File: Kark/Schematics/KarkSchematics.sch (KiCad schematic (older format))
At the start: 33 parts

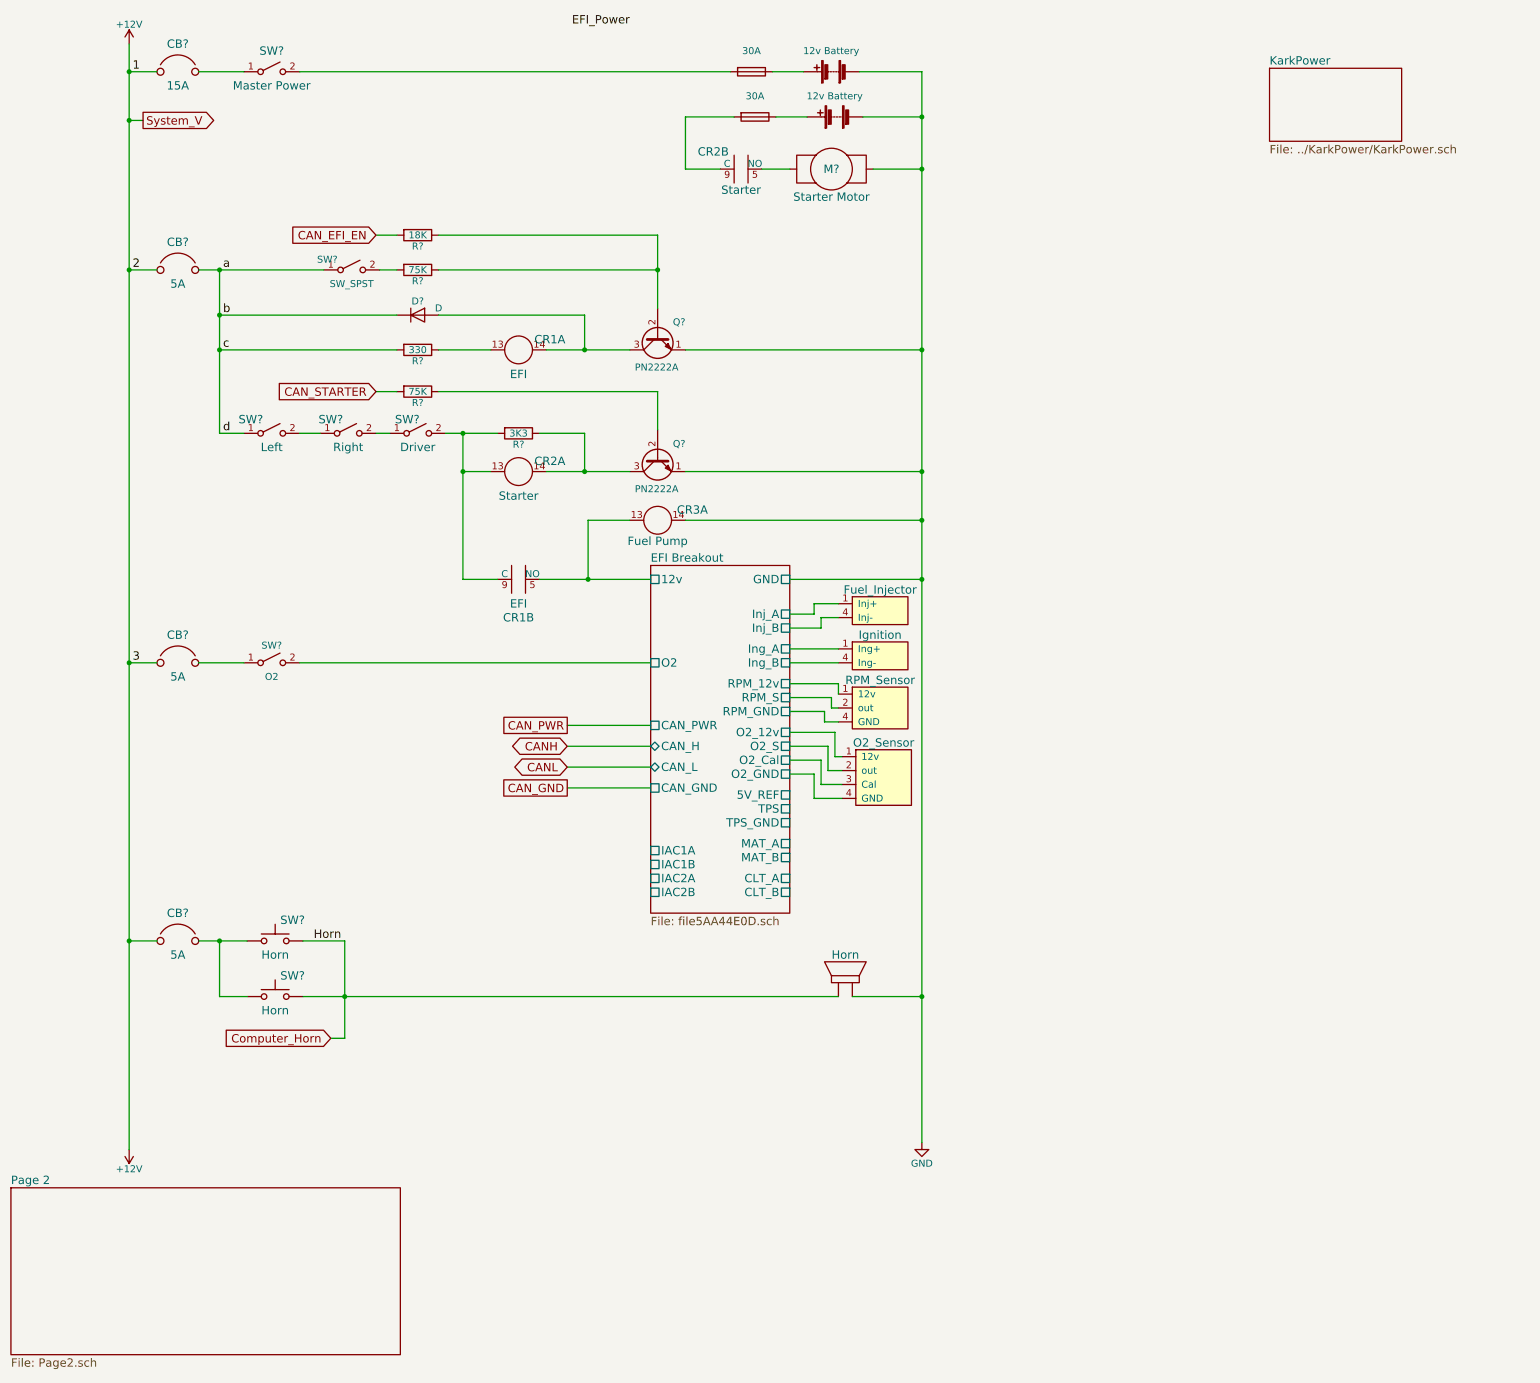
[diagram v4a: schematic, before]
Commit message: Created can breakout
Added can boards fro sensors and integrated the computer to the can system.
Created the Can powering system.
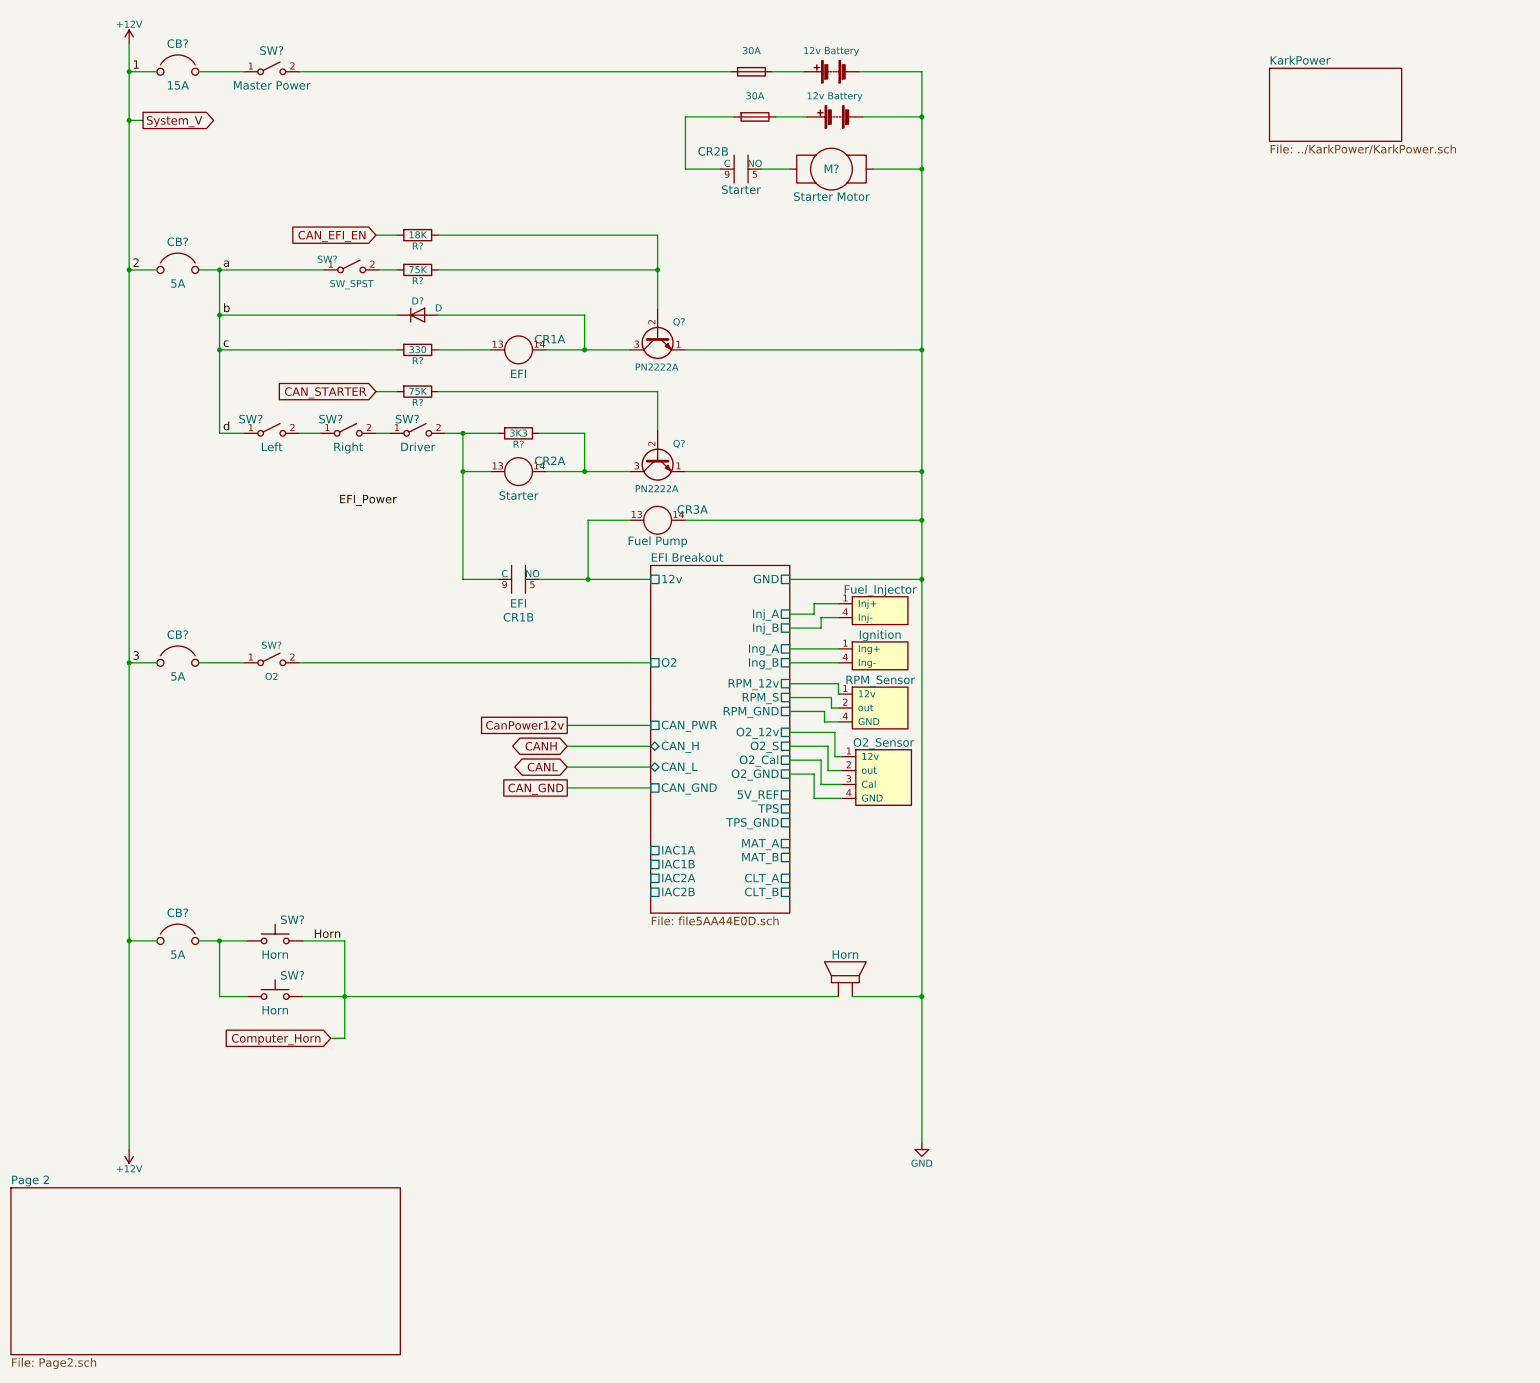
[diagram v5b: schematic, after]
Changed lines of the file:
@@
 LIBS:supermileage_computers
 LIBS:supermileage_sensors
+LIBS:EllicottDisplay
+LIBS:EllicottInterface
+LIBS:EllicottMicrocontrollers
+LIBS:EllicottMisc
+LIBS:EllicottPower
 LIBS:KarkSchematics-cache
 EELAYER 25 0
@@
 $Descr USLetter 8500 11000 portrait
 encoding utf-8
-Sheet 1 6
+Sheet 1 9
 Title "Kark - Gasoline Prototype"
 Date "2018-03-10"
@@
 Text Label 3025 7350 2    60   ~ 0
 Horn
-Text Label 5100 775  2    60   ~ 0
+Text Label 3425 4225 2    60   ~ 0
 EFI_Power
 $Sheet
@@
 CAN_GND
 Text GLabel 4650 5800 0    60   UnSpc ~ 0
-CAN_PWR
+CanPower12v
 Text GLabel 1600 1450 2    60   Output ~ 0
 System_V
@@
 Connection ~ 1500 2525
 Wire Wire Line
-	2150 2525 2150 2850
-Wire Wire Line
-	2150 2850 2150 3100
-Wire Wire Line
-	2150 3100 2150 3700
+	2150 2525 2150 3700
 Wire Wire Line
 	2750 7350 3050 7350
 Wire Wire Line
-	3050 7350 3050 7750
-Wire Wire Line
-	3050 7750 3050 8050
+	3050 7350 3050 8050
 Connection ~ 3050 7750
 Wire Wire Line
@@
 	6250 5350 6600 5350
 Wire Wire Line
-	2750 7750 3050 7750
-Wire Wire Line
-	3050 7750 6600 7750
+	2750 7750 6600 7750
 Wire Wire Line
 	7200 7750 6700 7750
 Wire Wire Line
-	7200 1100 7200 1425
-Wire Wire Line
-	7200 1425 7200 1800
-Wire Wire Line
-	7200 1800 7200 3100
-Wire Wire Line
-	7200 3100 7200 3975
-Wire Wire Line
-	7200 3975 7200 4325
-Wire Wire Line
-	7200 4325 7200 4750
-Wire Wire Line
-	7200 4750 7200 7750
-Wire Wire Line
-	7200 7750 7200 8800
+	7200 1100 7200 8800
 Wire Wire Line
 	5500 1800 5750 1800
@@
 Connection ~ 7200 1800
 Wire Wire Line
-	1500 900  1500 1100
-Wire Wire Line
-	1500 1100 1500 1450
-Wire Wire Line
-	1500 1450 1500 2525
-Wire Wire Line
-	1500 2525 1500 5350
-Wire Wire Line
-	1500 5350 1500 7350
-Wire Wire Line
-	1500 7350 1500 8850
+	1500 900  1500 8850
 Wire Wire Line
 	3050 8050 2950 8050
@@
 Connection ~ 1500 1450
 Wire Wire Line
-	3775 3700 3900 3700
-Wire Wire Line
-	3900 3700 4150 3700
+	3775 3700 4150 3700
 Wire Wire Line
 	3900 4750 4150 4750
@@
 	3425 3100 2150 3100
 Wire Wire Line
-	4500 3100 4775 3100
-Wire Wire Line
-	4775 3100 5100 3100
+	4500 3100 5100 3100
 Wire Wire Line
 	7200 3100 5500 3100
@@
 Connection ~ 4775 3100
 Wire Wire Line
-	2000 2525 2150 2525
-Wire Wire Line
-	2150 2525 2900 2525
+	2000 2525 2900 2525
 Wire Wire Line
 	3425 2525 3300 2525
@@
 	3725 2525 5300 2525
 Wire Wire Line
-	5300 2275 5300 2525
-Wire Wire Line
-	5300 2525 5300 2800
+	5300 2275 5300 2800
 Connection ~ 5300 2525
 Wire Wire Line
@@
 	2000 5350 2325 5350
 Wire Wire Line
-	2000 7350 2150 7350
-Wire Wire Line
-	2150 7350 2350 7350
+	2000 7350 2350 7350
 Wire Wire Line
 	1700 7350 1500 7350
@@
 $EndComp
 Wire Wire Line
-	4500 3975 4775 3975
-Wire Wire Line
-	4775 3975 5100 3975
+	4500 3975 5100 3975
 Text GLabel 3275 3400 0    60   Input ~ 0
 CAN_STARTER
@@
 	4100 3975 3900 3975
 Wire Wire Line
-	3900 3700 3900 3975
-Wire Wire Line
-	3900 3975 3900 4750
+	3900 3700 3900 4750
 Connection ~ 3900 3975
 Connection ~ 3900 3700
@@
 	6600 5250 6250 5250
 Wire Wire Line
-	4450 4750 4800 4750
-Wire Wire Line
-	4800 4750 5250 4750
+	4450 4750 5250 4750
 Wire Wire Line
 	4800 4750 4800 4325

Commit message: Finished Schematics
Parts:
- removed CB?: 5A, symbol CB
- removed SP?: Horn, symbol Horn
- removed SW? (x2): Horn, symbol SW_Push
- added CB104: 5A, symbol CB
- added unit 2 of CR3
- added D104: Brake Light, symbol LED_ALT
- added M102: Fuel Pump, symbol Motor
- gave numbers to parts that had none: 26
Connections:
- net +12V: now also CR1.9 (C), CR2.13, R109.2, SW106.2 (B), CB104.1 (Line)
- net GND: now also M102.2
- net at CR2.9 (C), F102.2: now also D104.2 (A)
- net EFI Breakout/12v renamed A
- new net: CR3.5 (NO), M102.1
- new net: CB104.2 (Load), CR3.9 (C)
- new net Brake_Light: D104.1 (K)
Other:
- moved on the sheet: CB102, CB103, CR1A, CR1B, CR2A, CR3A, D103, Q102, Q103, R105, R106, R107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

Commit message: removed files
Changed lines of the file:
@@
 U 1 1 5AA44DF4
 P 3075 4025
-F 0 "SW104" H 2950 4125 60  0000 C CNN
+F 0 "SW104" H 2925 4125 60  0000 C CNN
 F 1 "Right" H 3075 3925 60  0000 C CNN
 F 2 "" H 3075 4025 60  0000 C CNN
@@
 U 1 1 5AA44DF5
 P 3575 4025
-F 0 "SW106" H 3500 4125 60  0000 C CNN
+F 0 "SW106" H 3425 4125 60  0000 C CNN
 F 1 "Driver" H 3575 3925 60  0000 C CNN
 F 2 "" H 3575 4025 60  0000 C CNN
@@
 Text GLabel 4650 6125 0    60   UnSpc ~ 0
 CanPower12v
-Text GLabel 1600 1450 2    60   Output ~ 0
-System_V
 $Comp
 L SPDT_Relay CR1
@@
 U 1 1 5AADC3DC
 P 5300 3325
-F 0 "Q102" V 5200 3125 50  0000 L CNN
+F 0 "Q102" V 5200 3050 50  0000 L CNN
 F 1 "PN2222A" V 5525 3175 50  0000 L CNN
 F 2 "TO_SOT_Packages_THT:TO-92_Inline_Wide" H 5500 3250 50  0001 L CIN
@@
 Connection ~ 1500 2850
 Wire Wire Line
-	2150 2850 2150 3175
-Wire Wire Line
-	2150 3175 2150 3425
-Wire Wire Line
-	2150 3425 2150 4025
+	2150 2850 2150 4025
 Wire Wire Line
 	6575 6350 6575 6175
@@
 	6250 5675 6600 5675
 Wire Wire Line
-	7200 1100 7200 1425
-Wire Wire Line
-	7200 1425 7200 1800
-Wire Wire Line
-	7200 1800 7200 3425
-Wire Wire Line
-	7200 3425 7200 4300
-Wire Wire Line
-	7200 4300 7200 4650
-Wire Wire Line
-	7200 4650 7200 5075
-Wire Wire Line
-	7200 5075 7200 8000
-Wire Wire Line
-	7200 8000 7200 8800
+	7200 1100 7200 8800
 Wire Wire Line
 	5500 1800 5750 1800
@@
 Connection ~ 7200 1800
 Wire Wire Line
-	1500 900  1500 1100
-Wire Wire Line
-	1500 1100 1500 1450
-Wire Wire Line
-	1500 1450 1500 2850
-Wire Wire Line
-	1500 2850 1500 5675
-Wire Wire Line
-	1500 5675 1500 8000
-Wire Wire Line
-	1500 8000 1500 8850
+	1500 900  1500 8850
 Wire Wire Line
 	4650 6275 5250 6275
@@
 	6150 1100 6350 1100
 Wire Wire Line
-	1600 1450 1500 1450
-Connection ~ 1500 1450
-Wire Wire Line
-	3775 4025 3900 4025
-Wire Wire Line
-	3900 4025 4150 4025
+	3775 4025 4150 4025
 Wire Wire Line
 	3900 4650 4150 4650
@@
 	3425 3425 2150 3425
 Wire Wire Line
-	4500 3425 4800 3425
-Wire Wire Line
-	4800 3425 5100 3425
+	4500 3425 5100 3425
 Wire Wire Line
 	7200 3425 5500 3425
@@
 Connection ~ 4800 3425
 Wire Wire Line
-	2000 2850 2150 2850
-Wire Wire Line
-	2150 2850 2900 2850
+	2000 2850 2900 2850
 Wire Wire Line
 	3425 2850 3300 2850
@@
 	3725 2850 5300 2850
 Wire Wire Line
-	5300 2600 5300 2850
-Wire Wire Line
-	5300 2850 5300 3125
+	5300 2600 5300 3125
 Connection ~ 5300 2850
 Wire Wire Line
@@
 	5500 1425 5850 1425
 Wire Wire Line
-	5500 1425 5500 1800
-Wire Wire Line
-	5500 1800 5500 2275
+	5500 1425 5500 2275
 Wire Wire Line
 	2150 4025 2325 4025
@@
 U 1 1 5AB6BF51
 P 5300 4200
-F 0 "Q103" V 5200 4000 50  0000 L CNN
+F 0 "Q103" V 5200 3925 50  0000 L CNN
 F 1 "PN2222A" V 5525 4050 50  0000 L CNN
 F 2 "TO_SOT_Packages_THT:TO-92_Inline_Wide" H 5500 4125 50  0001 L CIN
@@
 $EndComp
 Wire Wire Line
-	4500 4300 4800 4300
-Wire Wire Line
-	4800 4300 5100 4300
+	4500 4300 5100 4300
 Text GLabel 3275 3725 0    60   Input ~ 0
 CAN_STARTER
@@
 	4100 4300 3900 4300
 Wire Wire Line
-	3900 4025 3900 4300
-Wire Wire Line
-	3900 4300 3900 4650
+	3900 4025 3900 4650
 Connection ~ 3900 4300
 Connection ~ 3900 4025
@@
 	4800 5075 4800 4650
 Wire Wire Line
-	4450 4650 4800 4650
-Wire Wire Line
-	4800 4650 5100 4650
+	4450 4650 5100 4650
 Wire Wire Line
 	5500 4650 7200 4650

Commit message: Added EFI Breakout File
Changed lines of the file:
@@
 U 5AA44E0D
 F0 "EFI Breakout" 60
-F1 "file5AA44E0D.sch" 60
+F1 "EFI_Breakout.sch" 60
 F2 "12v" U L 5250 5075 60
 F3 "GND" U R 6250 5075 60
